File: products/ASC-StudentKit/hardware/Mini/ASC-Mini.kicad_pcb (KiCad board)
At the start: 2 copper layers, 97.4 x 47 mm, 92 parts, among them J1 12V IN, J10 OUT2, J2 USB-C, J3 PROG (pogo pads), J4 S1, J5 S2, J6 S3, J7 S4, J8 I2C-1 (Grove), J9 OUT1, K1 HF46F/005-HS1, K2 HF46F/005-HS1, Q1 AO3400A, Q2 AO3400A, Q3 AO3400A, SW1 RESET, SW2 PAIR / BOOT, U1 ESP32-S3-MINI-1-N8, U2 TPS54202DDC, U3 USBLC6-2SC6, U4 AP7361C-33E, U5 DS3231MZ+

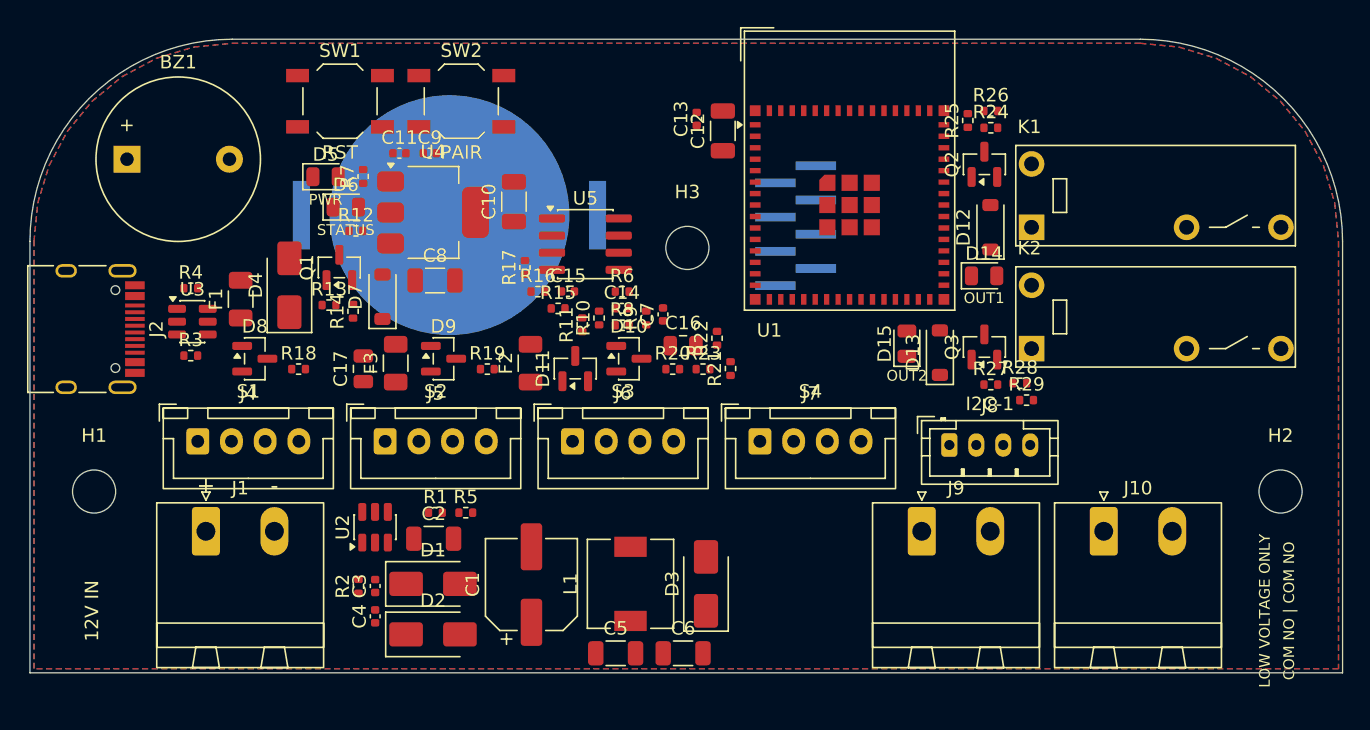
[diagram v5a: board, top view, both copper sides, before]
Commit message: Mini PCB: fix back-side parts in the DSN export; copper connectivity check
route.py gave Specctra the back-side parts' front view and let it mirror
them, which put J3's (asymmetric) pads at mirrored positions, so every J3
net came back split. Back parts now go in exactly as the board file has
them, placed front with their pads on B.Cu. (BT1 hid the bug: it is
symmetric.)

tools/check_connect.py traces every net through pads, tracks and vias
and lists any split net with the pads in each piece; it found the bug.
The board in this commit is the variant-a import before the fix.

Co-Authored-By: Claude Opus 5.5 <noreply@anthropic.com>
Claude-Session: https://claude.ai/code/session_0137TCDSR58nWZn1byy7MgSb
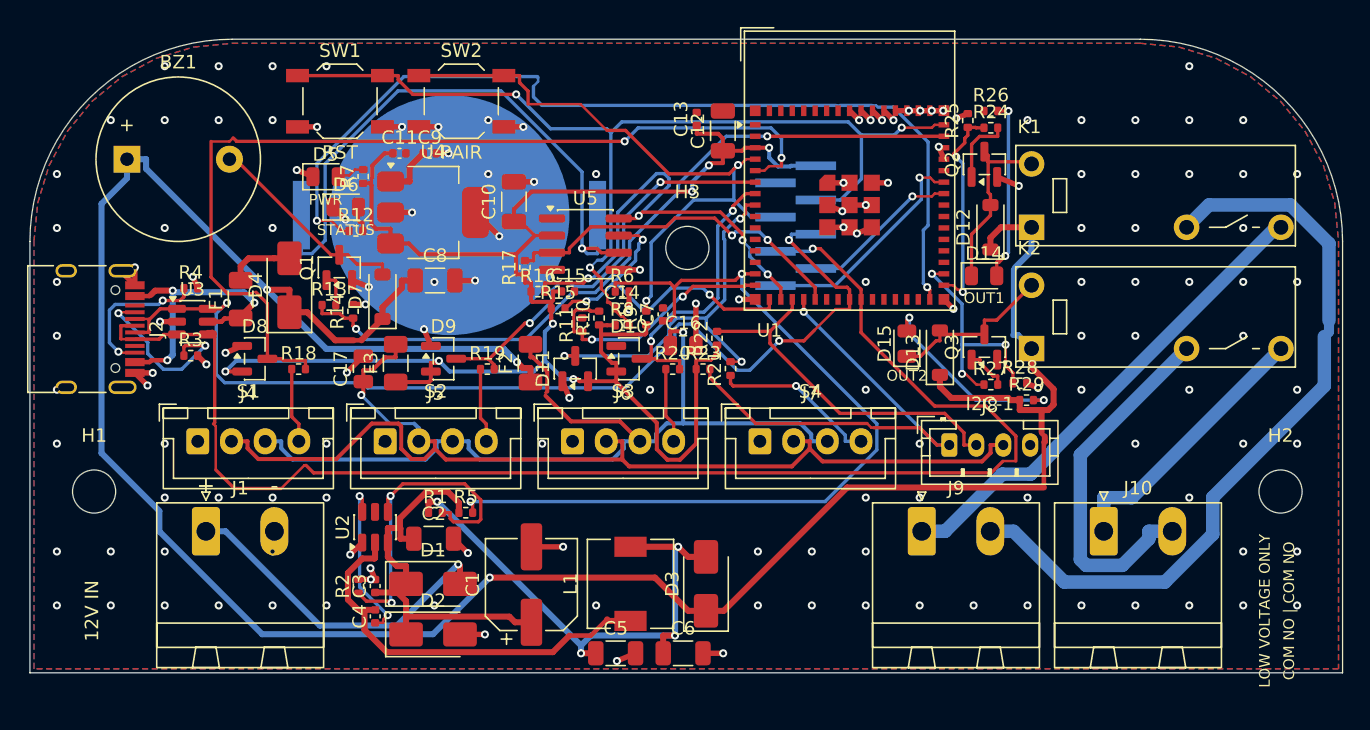
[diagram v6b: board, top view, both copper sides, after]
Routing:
- net +5V: track 0.00 -> 199.3 mm, vias 0 -> 3
- net +3V3: track 0.00 -> 132.7 mm, vias 0 -> 7
- net /USB_DP: track 0.00 -> 108.3 mm, vias 0 -> 1
- net /+3V3_PORT: track 0.00 -> 81.8 mm, vias 0 -> 1
- net /USB_DN: track 0.00 -> 77.9 mm, vias 0 -> 3
- net /EN: track 0.00 -> 74.7 mm, vias 0 -> 3
- net GND: track 0.00 -> 72.6 mm, vias 0 -> 149
- net /LED: track 0.00 -> 70.3 mm, vias 0 -> 2
- net /S1: track 0.00 -> 70.2 mm, vias 0 -> 2
- net /+5V_PORT: track 0.00 -> 68.7 mm, vias 0 -> 1
- net /VIN_SENSE: track 0.00 -> 64.6 mm, vias 0 -> 2
- net /OUT1_NO: track 0.00 -> 57.1 mm
- net /BUZZER: track 0.00 -> 55.2 mm, vias 0 -> 2
- net /PAIR: track 0.00 -> 48.4 mm, vias 0 -> 2
- net /VBAT_RTC: track 0.00 -> 47.2 mm, vias 0 -> 1
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
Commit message: Mini PCB: every signal net routed; grid router and clearance check
Signals: Freerouting variant e (power 0.45, supply 0.3, clearance 0.19,
via 0.55) left +5V in three pieces; tools/patch_route.py, a two-layer A*
grid router (0.2 mm grid, width-aware clearance masks, vias), joined them
with 0.45 mm tracks and 5 vias. check_connect.py: every net joined by
copper (GND still to do).

tools/check_clearance.py: a DRC subset (tracks, vias and pads of
different nets per layer, board edge, mounting holes). The board passes
at 0.18 mm; the closest gap is 0.192 mm.

Co-Authored-By: Claude Opus 5.5 <noreply@anthropic.com>
Claude-Session: https://claude.ai/code/session_0137TCDSR58nWZn1byy7MgSb
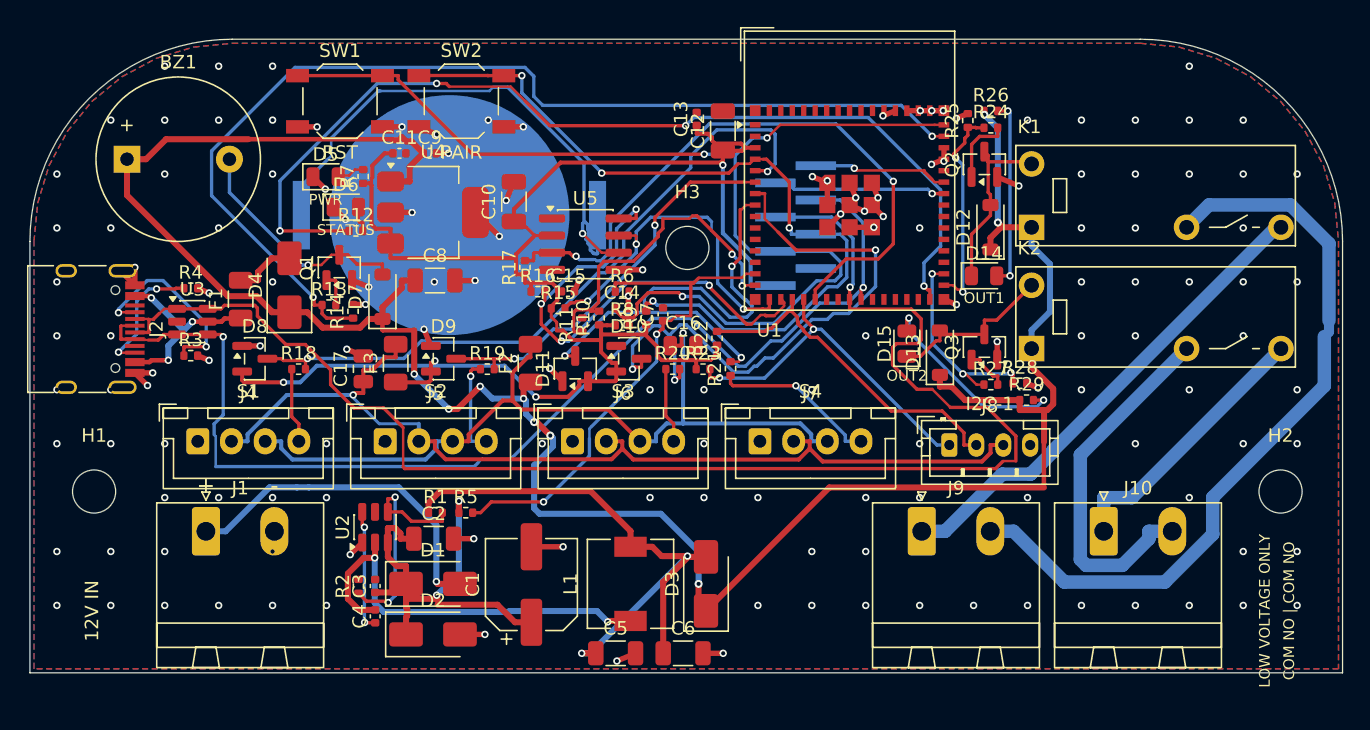
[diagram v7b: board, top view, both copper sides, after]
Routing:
- net /USB_DN: track 77.9 -> 111.5 mm, vias 3 -> 1
- net /VIN_SENSE: track 64.6 -> 38.7 mm
- net /S3: track 20.7 -> 45.5 mm, vias 2 -> 3
- net +5V: track 199.3 -> 175.1 mm, vias 3 -> 9
- net /BUZZER: track 55.2 -> 78.1 mm
- net /USB_DP: track 108.3 -> 86.3 mm, vias 1 -> 2
- net /RTC_INT: track 26.6 -> 47.9 mm
- net /S1: track 70.2 -> 51.0 mm
- net /EN: track 74.7 -> 88.6 mm
- net /PAIR: track 48.4 -> 61.4 mm, vias 2 -> 4
- net /I2C1_SCL: track 36.3 -> 26.0 mm, vias 1 -> 2
- net /S4: track 28.6 -> 37.8 mm
- net /+3V3_PORT: track 81.8 -> 74.1 mm
- net /BUCK_FB: track 24.4 -> 17.1 mm
- net /VBUS: track 21.9 -> 14.5 mm
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
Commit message: Mini PCB: GND routed as tracks; rip-up and reroute in patch_route.py
GND stage (Freerouting, variant ga) plus patch_route.py: GND is now one
piece of copper except 4 pads (C7, R11, U1.63, U5.5). patch_route.py
gains rip-up and reroute: when no free path exists, the path may cross
other nets' copper at a cost, the crossed tracks are removed, GND goes in,
and the moved nets are re-routed; if any can't be, everything rolls back.
A via along a track (not only at its end) now counts as joined, in both
patch_route.py and check_connect.py. Patch vias are 0.55 mm, the size
Freerouting was given.

Checks: every signal net joined; clearance OK at 0.18 mm.

Co-Authored-By: Claude Opus 5.5 <noreply@anthropic.com>
Claude-Session: https://claude.ai/code/session_0137TCDSR58nWZn1byy7MgSb
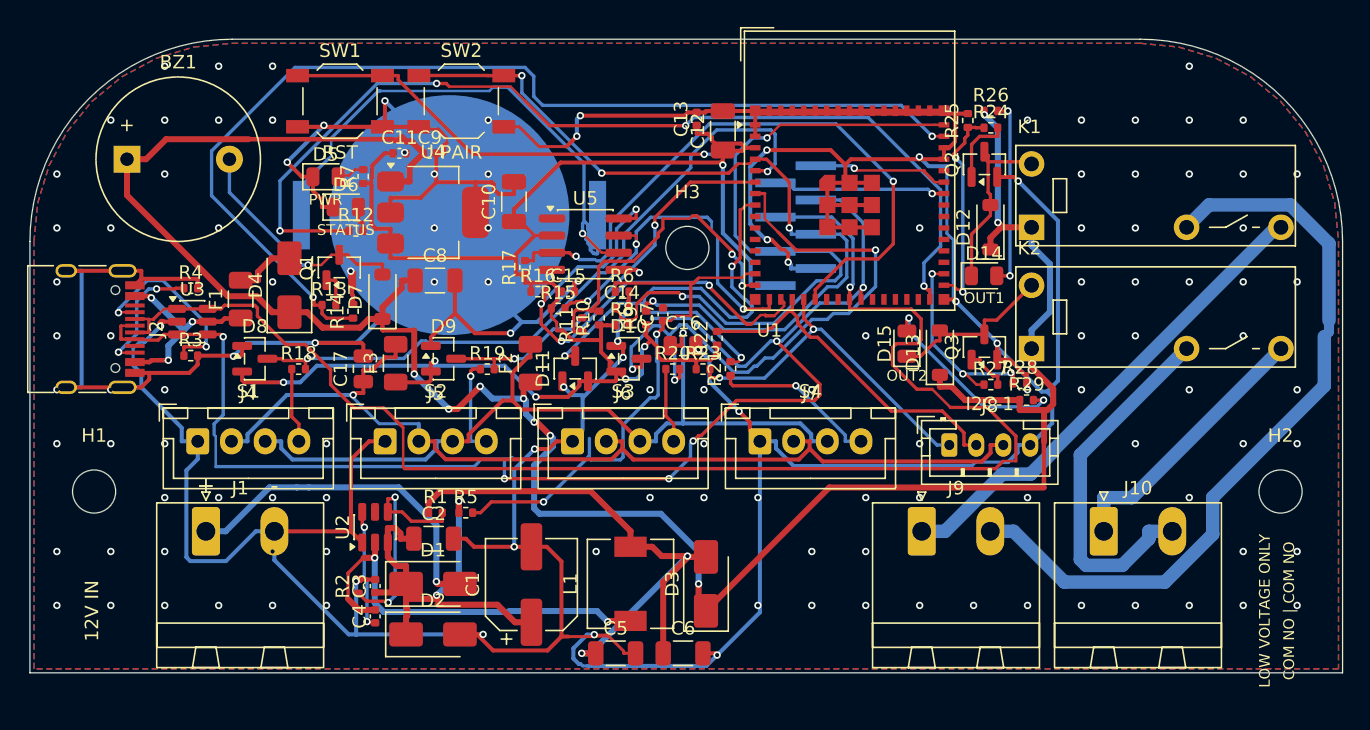
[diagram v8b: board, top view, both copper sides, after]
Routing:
- net GND: track 67.6 -> 486.0 mm, vias 151 -> 139
- net /USB_DP: track 86.3 -> 105.0 mm, vias 2 -> 6
- net /VIN_SENSE: track 38.7 -> 42.2 mm
- net +3V3: track 129.9 -> 130.7 mm, vias 4 -> 6
